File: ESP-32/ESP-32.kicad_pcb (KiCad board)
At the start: 2 copper layers, 36 parts, among them J1 USB_B_Micro, J2 Conn_01x21_Pin, J3 Conn_01x21_Pin, Q1 2SC4213, Q2 2SC4213, SW1 SW_Omron_B3FS, SW2 SW_Omron_B3FS, U1 CP2102N-Axx-xQFN28, U2 esp32-devkitM-1, U3 LM1117MP-3.3

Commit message: OTRA VEX
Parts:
- moved R7 3.59 mm to (156.5, 63.5)
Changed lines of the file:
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@@
   )
   (footprint "Resistor_SMD:R_0805_2012Metric_Pad1.20x1.40mm_HandSolder" (layer "F.Cu")
-    (at 153.94 60.96)
+    (at 156.48 63.5)
     (descr "Resistor SMD 0805 (2012 Metric), square (rectangular) end terminal, IPC_7351 nominal with elongated pad for handsoldering. (Body size source: IPC-SM-782 page 72, https://www.pcb-3d.com/wordpress/wp-content/uploads/ipc-sm-782a_amendment_1_and_2.pdf), generated with kicad-footprint-generator")
     (tags "resistor handsolder")

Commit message: DSD
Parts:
- moved D1 3.59 mm to (106.7, 66.0)
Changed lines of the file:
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@@
   )
   (footprint "Diode_THT:D_DO-41_SOD81_P10.16mm_Horizontal" (layer "F.Cu")
-    (at 109.22 68.58)
+    (at 106.68 66.04)
     (descr "Diode, DO-41_SOD81 series, Axial, Horizontal, pin pitch=10.16mm, , length*diameter=5.2*2.7mm^2, , http://www.diodes.com/_files/packages/DO-41%20(Plastic).pdf")
     (tags "Diode DO-41_SOD81 series Axial Horizontal pin pitch 10.16mm  length 5.2mm diameter 2.7mm")

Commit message: fxg
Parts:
- moved D1 5.68 mm to (111.8, 68.6)
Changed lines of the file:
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@@
   )
   (footprint "Diode_THT:D_DO-41_SOD81_P10.16mm_Horizontal" (layer "F.Cu")
-    (at 106.68 66.04)
+    (at 111.76 68.58)
     (descr "Diode, DO-41_SOD81 series, Axial, Horizontal, pin pitch=10.16mm, , length*diameter=5.2*2.7mm^2, , http://www.diodes.com/_files/packages/DO-41%20(Plastic).pdf")
     (tags "Diode DO-41_SOD81 series Axial Horizontal pin pitch 10.16mm  length 5.2mm diameter 2.7mm")

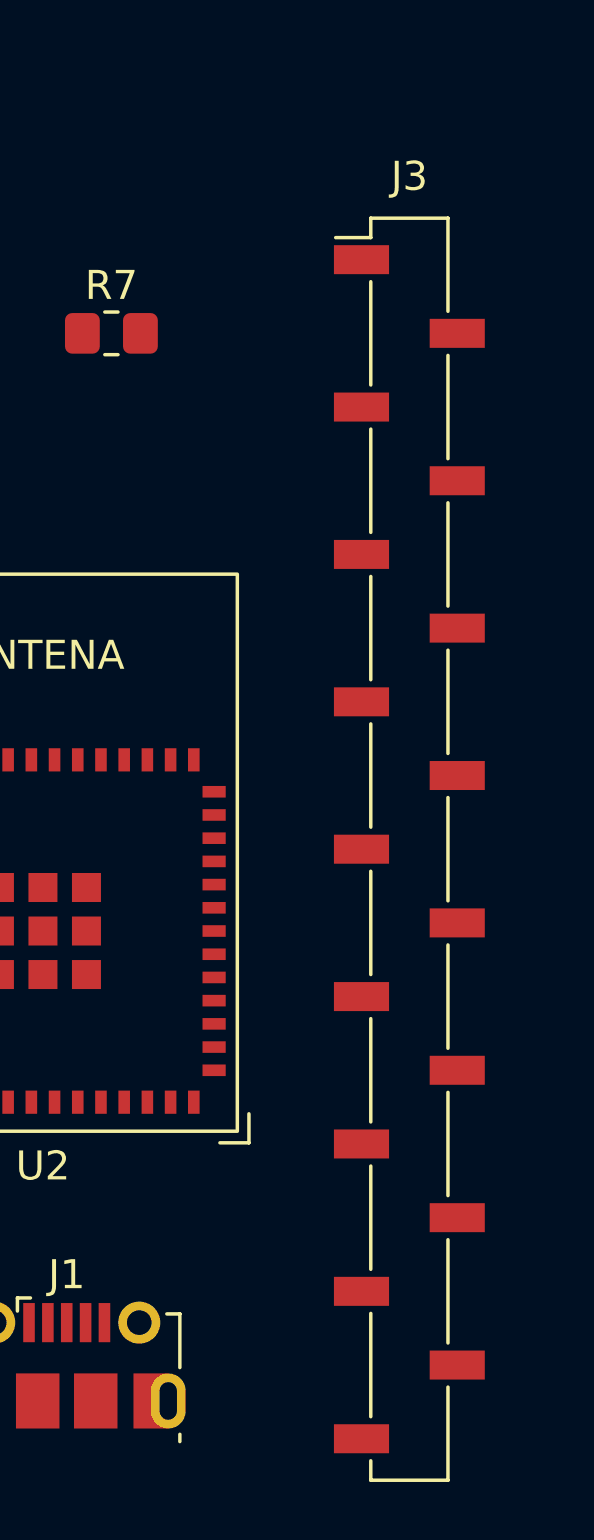
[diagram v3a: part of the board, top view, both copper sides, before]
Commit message: Se ha añadido el diseño pcb
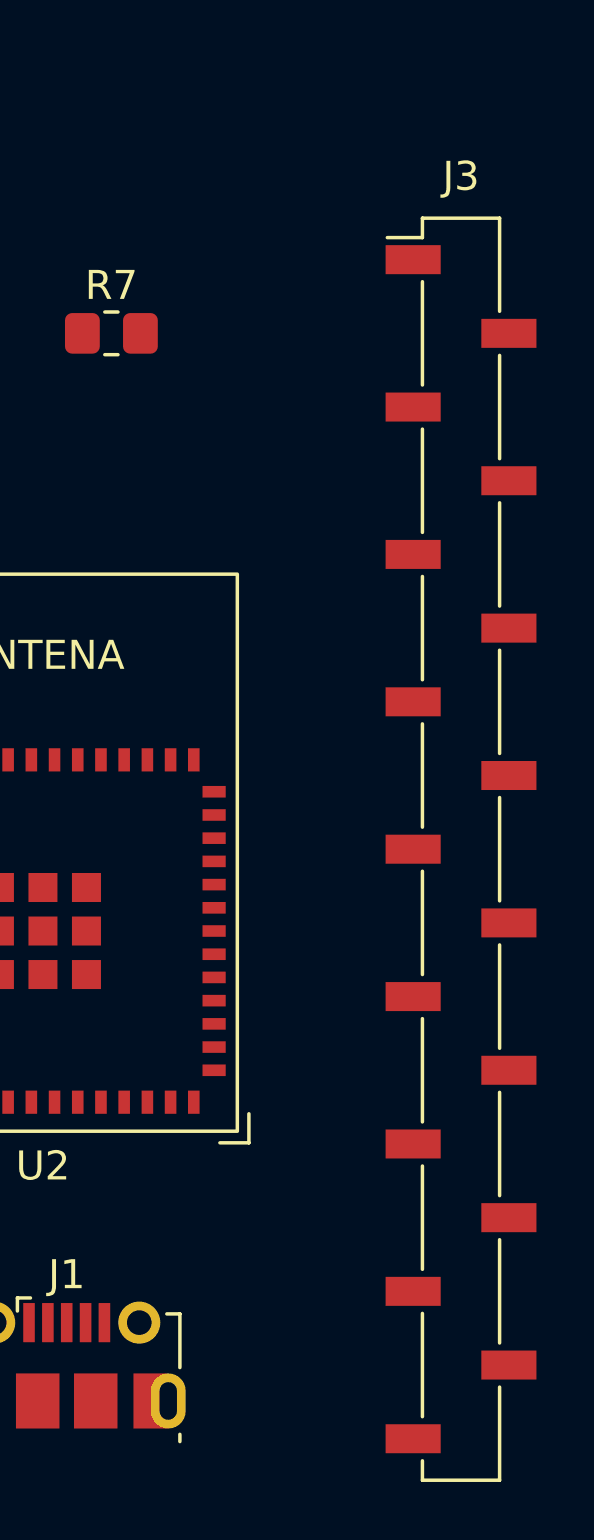
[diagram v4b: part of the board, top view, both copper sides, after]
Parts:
- moved J3 1.78 mm to (168.5, 81.3)
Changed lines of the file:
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@@
   )
   (footprint "Connector_PinSocket_2.54mm:PinSocket_1x17_P2.54mm_Vertical_SMD_Pin1Left" (layer "F.Cu")
-    (at 166.75 81.28)
+    (at 168.53 81.28)
     (descr "surface-mounted straight socket strip, 1x17, 2.54mm pitch, single row, style 1 (pin 1 left) (https://cdn.harwin.com/pdfs/M20-786.pdf), script generated")
     (tags "Surface mounted socket strip SMD 1x17 2.54mm single row style1 pin1 left")

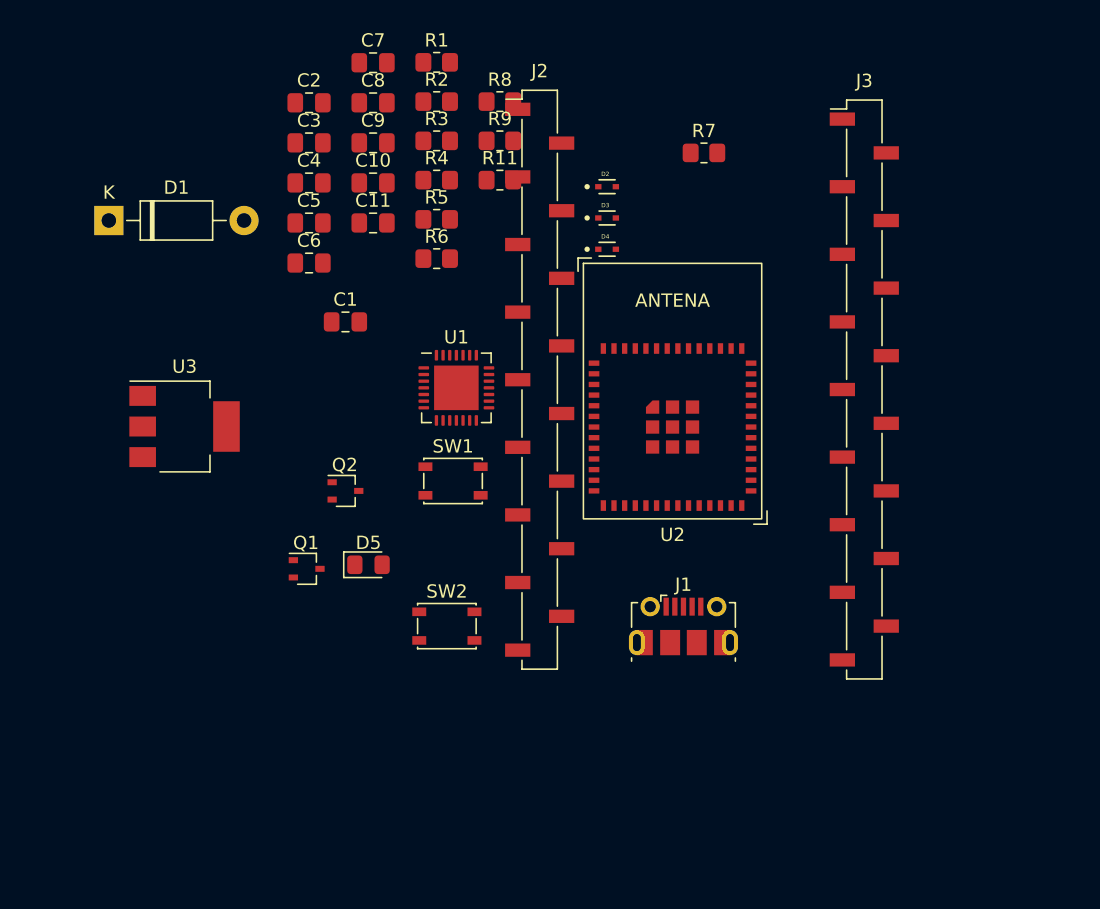
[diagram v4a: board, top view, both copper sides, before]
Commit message: pcb actualizado
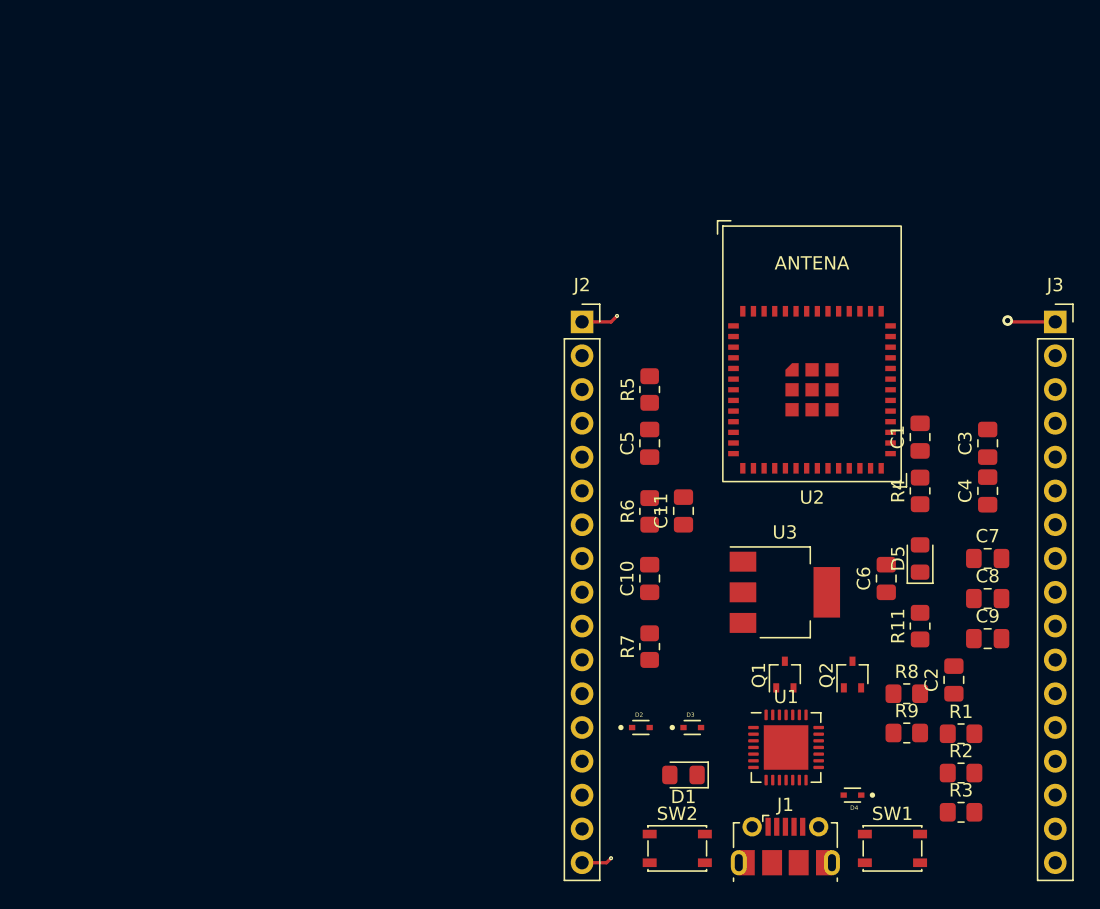
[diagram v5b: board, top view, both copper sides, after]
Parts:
- D1: footprint Diode_THT:D_DO-41_SOD81_P10.16mm_Horizontal -> Diode_SMD:D_0805_2012Metric_Pad1.15x1.40mm_HandSolder
- J2, J3: footprint Connector_PinSocket_2.54mm:PinSocket_1x17_P2.54mm_Vertical_SMD_Pin1Left -> Connector_PinSocket_2.54mm:PinSocket_1x17_P2.54mm_Vertical
- moved C2 65.0 mm to (175.3, 103.1), turned to 90 degrees
- moved R1 64.0 mm to (175.8, 107.2)
- moved R2 64.0 mm to (175.8, 110.1)
- moved R3 64.0 mm to (175.8, 113.0)
- moved D1 60.0 mm to (154.9, 110.2), turned to 180 degrees
- moved C7 59.3 mm to (177.8, 94.0)
- moved C8 59.3 mm to (177.8, 97.0)
- moved C9 59.3 mm to (177.8, 100.0)
- moved C4 56.0 mm to (177.8, 88.9), turned to 90 degrees
- moved C3 55.8 mm to (177.8, 85.3), turned to 90 degrees
- moved R9 54.0 mm to (171.7, 107.1)
- moved R8 54.0 mm to (171.7, 104.1)
- moved C6 49.4 mm to (170.2, 95.5), turned to 90 degrees
- moved U3 46.8 mm to (162.6, 96.5)
- moved R11 46.0 mm to (172.7, 99.1), turned to 90 degrees
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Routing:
- net GND: track 0.00 -> 8.76 mm, vias 0 -> 3
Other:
- copper layers 2 -> 4
